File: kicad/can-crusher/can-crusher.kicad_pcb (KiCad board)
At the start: 2 copper layers, 100 x 100 mm, 26 parts, among them J1 Stepper Right, J2 Control UART, J3 Ext power, J4 Stepper Left, J5 Barrel_Jack, J6 Expansion Port, Q1 IRF9540N, Q2 MMBF170, SW1 Reboot, SW2 User Interaction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

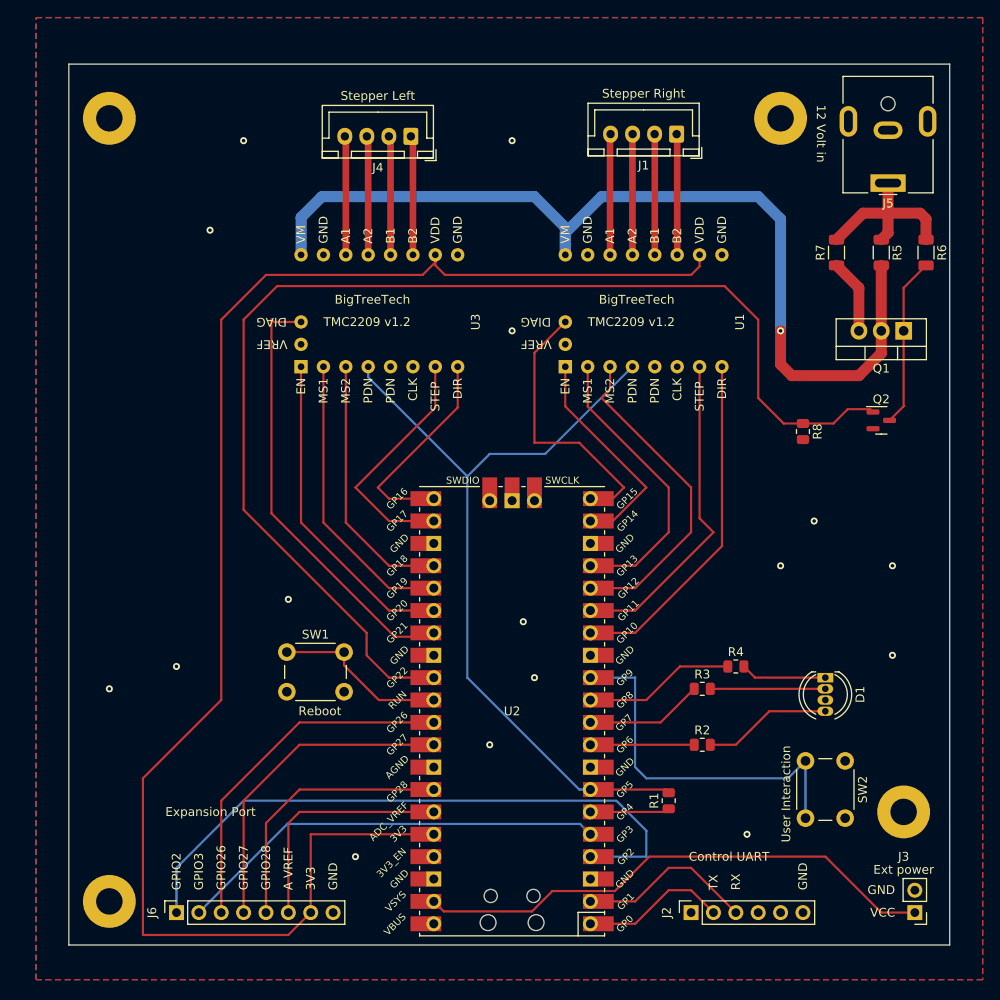
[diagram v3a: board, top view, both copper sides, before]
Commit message: Add fuse, power switch, and electrolytic caps
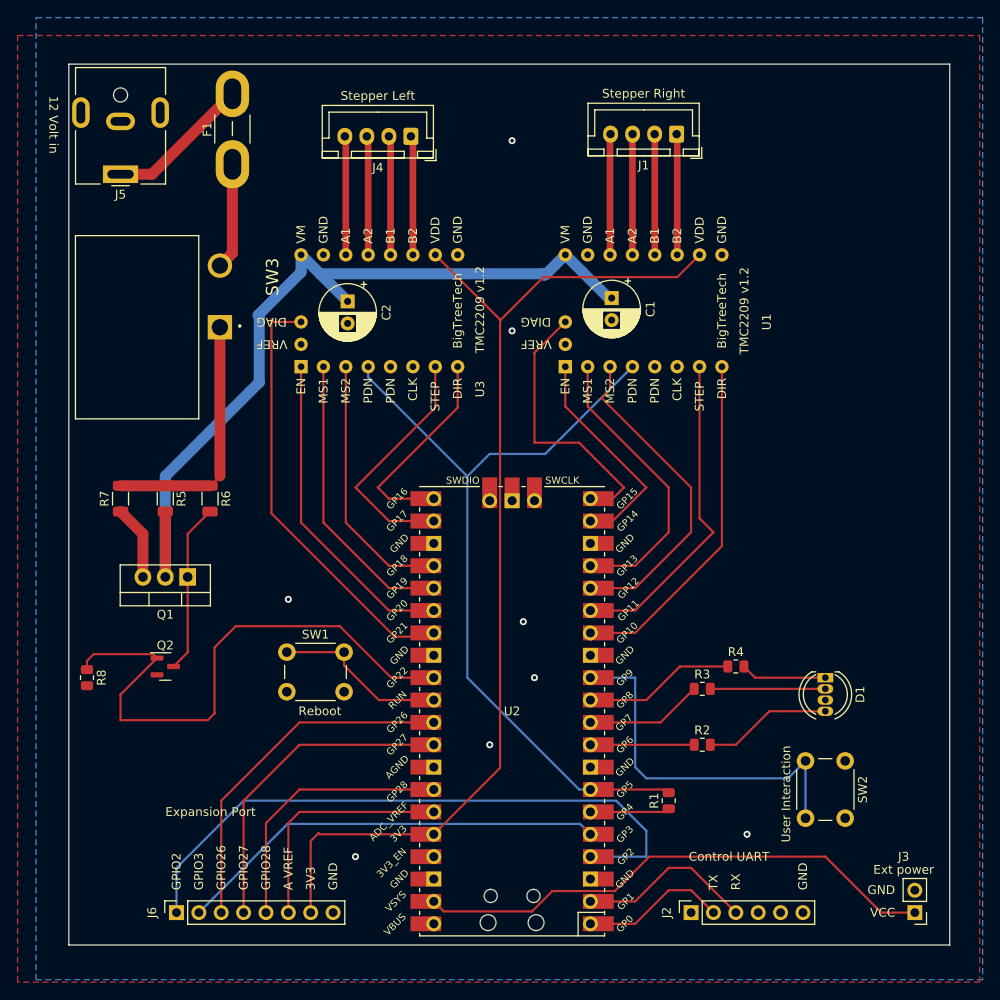
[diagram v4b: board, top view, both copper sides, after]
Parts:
- removed REF1, REF2, REF3, REF4: MountingHole_3mm_Pad, MountingHole:MountingHole_3mm_Pad
- added C1: C_Polarized, Capacitor_THT:CP_Radial_D6.3mm_P2.50mm, F.Cu at (158.6, 77.6)
- added C2: C_Polarized, Capacitor_THT:CP_Radial_D6.3mm_P2.50mm, F.Cu at (128.7, 77.9)
- added F1: Fuse, Fuse:Fuse_Blade_Mini_directSolder, F.Cu at (115.6, 62.4)
- added SW3: SW_SPST, R1966:SW_R1966ABLKBLKGR, F.Cu at (114.2, 80.9)
- moved J5 87.1 mm to (102.9, 63.5)
- moved Q1 85.9 mm to (110.5, 109.2)
- moved R6 85.9 mm to (113.0, 100.3)
- moved R7 85.9 mm to (102.9, 100.3)
- moved R8 85.9 mm to (99.1, 120.7)
- moved Q2 85.9 mm to (108.0, 119.4)
- moved R5 85.9 mm to (108.0, 100.3)
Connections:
- J5 pad 1: +12V -> Net-(F1-Pad2)
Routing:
- net Net-(Q2-Pad1): track 138.1 -> 65.0 mm
- net +3.3V: track 177.7 -> 120.2 mm
- net Net-(F1-Pad2): track 0.00 -> 16.5 mm
- net /12V_ON: track 109.0 -> 94.1 mm, vias 1 -> 0
- net Net-(F1-Pad1): track 0.00 -> 12.1 mm
- net +12V: track 20.8 -> 28.6 mm
- net GND: vias 16 -> 8

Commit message: Remove RGB led and button; add free pins to header; add ADC pins to the TMC2209 VREF pins for future use
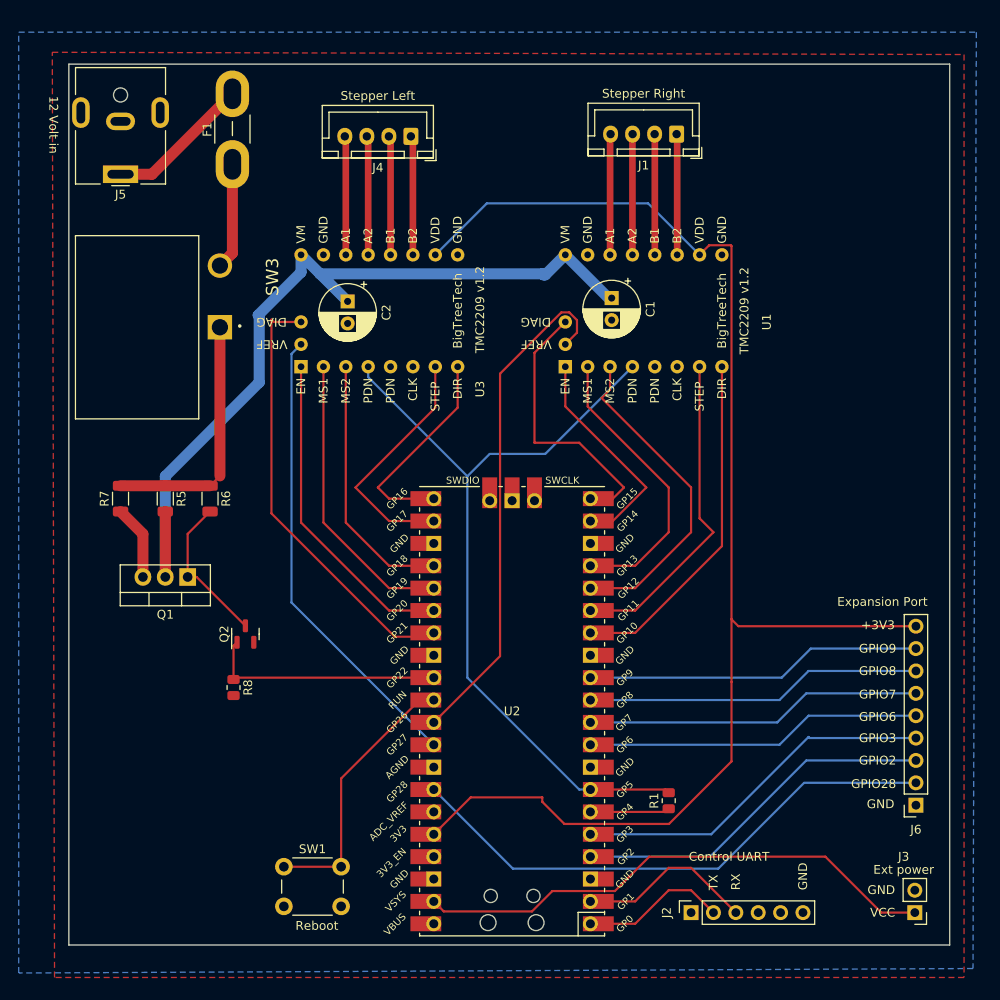
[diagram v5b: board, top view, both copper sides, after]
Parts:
- removed D1: LED_BRKG, LED_THT:LED_D5.0mm-4_RGB
- removed R2, R3, R4: 220, Resistor_SMD:R_0805_2012Metric
- removed SW2: User Interaction, Button_Switch_THT:SW_PUSH_6mm_H4.3mm
- J6: footprint Connector_PinSocket_2.54mm:PinSocket_1x08_P2.54mm_Vertical -> Connector_PinSocket_2.54mm:PinSocket_1x09_P2.54mm_Vertical
- moved J6 84.8 mm to (193.2, 135.1), turned to 180 degrees
- moved SW1 24.4 mm to (121.4, 142.1)
- moved R8 16.7 mm to (115.7, 121.8)
- moved Q2 9.81 mm to (117.0, 115.7), turned to 90 degrees
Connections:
- J6 pad 1: Net-(J6-Pad1) -> GND
- J6 pad 7: +3.3V -> Net-(J6-Pad7)
- J6 pad 8: GND -> Net-(J6-Pad8)
- U1 pad 18: unconnected-(U1-Pad18) -> Net-(U1-Pad18)
- U2 pad 10: Net-(R3-Pad1) -> Net-(J6-Pad6)
- U2 pad 11: Net-(R4-Pad1) -> Net-(J6-Pad7)
- U2 pad 12: Net-(SW2-Pad2) -> Net-(J6-Pad8)
- U2 pad 31: Net-(J6-Pad3) -> Net-(U1-Pad18)
- U2 pad 32: Net-(J6-Pad4) -> Net-(U2-Pad32)
- U2 pad 34: Net-(J6-Pad5) -> Net-(J6-Pad2)
- U2 pad 35: Net-(J6-Pad6) -> unconnected-(U2-Pad35)
- U2 pad 4: Net-(J6-Pad1) -> Net-(J6-Pad3)
- U2 pad 5: Net-(J6-Pad2) -> Net-(J6-Pad4)
- U2 pad 9: Net-(R2-Pad1) -> Net-(J6-Pad5)
- U3 pad 18: unconnected-(U3-Pad18) -> Net-(U2-Pad32)
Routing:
- net Net-(J6-Pad1): track 72.3 -> 0.00 mm
- net Net-(U1-Pad18): track 0.00 -> 58.0 mm
- net Net-(U2-Pad32): track 0.00 -> 52.6 mm
- net Net-(SW2-Pad2): track 42.4 -> 0.00 mm
- net +3.3V: track 120.2 -> 158.8 mm
- net Net-(J6-Pad8): track 0.00 -> 38.3 mm
- net Net-(J6-Pad7): track 0.00 -> 38.3 mm
- net Net-(Q2-Pad1): track 65.0 -> 27.2 mm
- net Net-(R4-Pad1): track 17.2 -> 0.00 mm
- net Net-(D1-Pad4): track 14.6 -> 0.00 mm
- net Net-(J6-Pad2): track 49.1 -> 62.5 mm
- net Net-(R3-Pad1): track 13.4 -> 0.00 mm
- net Net-(D1-Pad2): track 13.1 -> 0.00 mm
- net Net-(R2-Pad1): track 11.8 -> 0.00 mm
- net Net-(J6-Pad6): track 27.2 -> 38.3 mm
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
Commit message: Rev 2 of control PCB
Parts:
- removed F1: Fuse, Fuse:Fuse_Blade_Mini_directSolder
- added C3: 100 uF, Capacitor_THT:CP_Radial_D6.3mm_P2.50mm, F.Cu at (118.7, 132.5)
- added C4: 330 uF, Capacitor_Tantalum_SMD:CP_EIA-7343-43_Kemet-X, F.Cu at (104.5, 145.7)
- added D1: 1N5819WS, Diode_SMD:D_SOD-323, F.Cu at (105.0, 140.5)
- added L1: 330 uH, Inductor_THT:L_Radial_D12.0mm_P5.00mm_Fastron_11P, F.Cu at (106.8, 129.7)
- added U4: LM2575-5.0BU, Package_TO_SOT_SMD:TO-263-5_TabPin3, F.Cu at (118.8, 141.9)
- added X1: 3522-2, 3522:FUSE_3522-2, F.Cu at (108.2, 69.0)
- C1, C2: value C_Polarized -> 100 uF
- moved SW1 75.4 mm to (182.1, 97.4)
- moved SW3 3.69 mm to (113.9, 84.6)
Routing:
- net VCC: track 60.3 -> 121.0 mm
- net +12V: track 28.6 -> 74.8 mm
- net Net-(SW1-Pad1): track 30.7 -> 68.7 mm, vias 0 -> 1
- net Net-(D1-Pad1): track 0.00 -> 18.2 mm
- net Net-(J5-Pad1): track 16.5 -> 11.7 mm
- net Net-(SW3-Pad1): track 12.1 -> 13.9 mm
- net GND: vias 0 -> 51
